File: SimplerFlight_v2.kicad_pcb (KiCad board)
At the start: 2 copper layers, 93.8 x 73.5 mm, 77 parts, among them J1 Battery 1, J11 Servo, J13 SWD Header, J14 DM3CS-SF, J2 Encoder, J7 Battery 2, J8 USB, Q2 NPN, SW1 Boot Switch, SW2 System Reset, U1 AMS1117-3.3, U2 STM32F401RETx, U3 BMP581, U4 BNO085, U5 TPS56A37RPAR, U7 MX25V4006EM1I-13G, Y2 Crystal

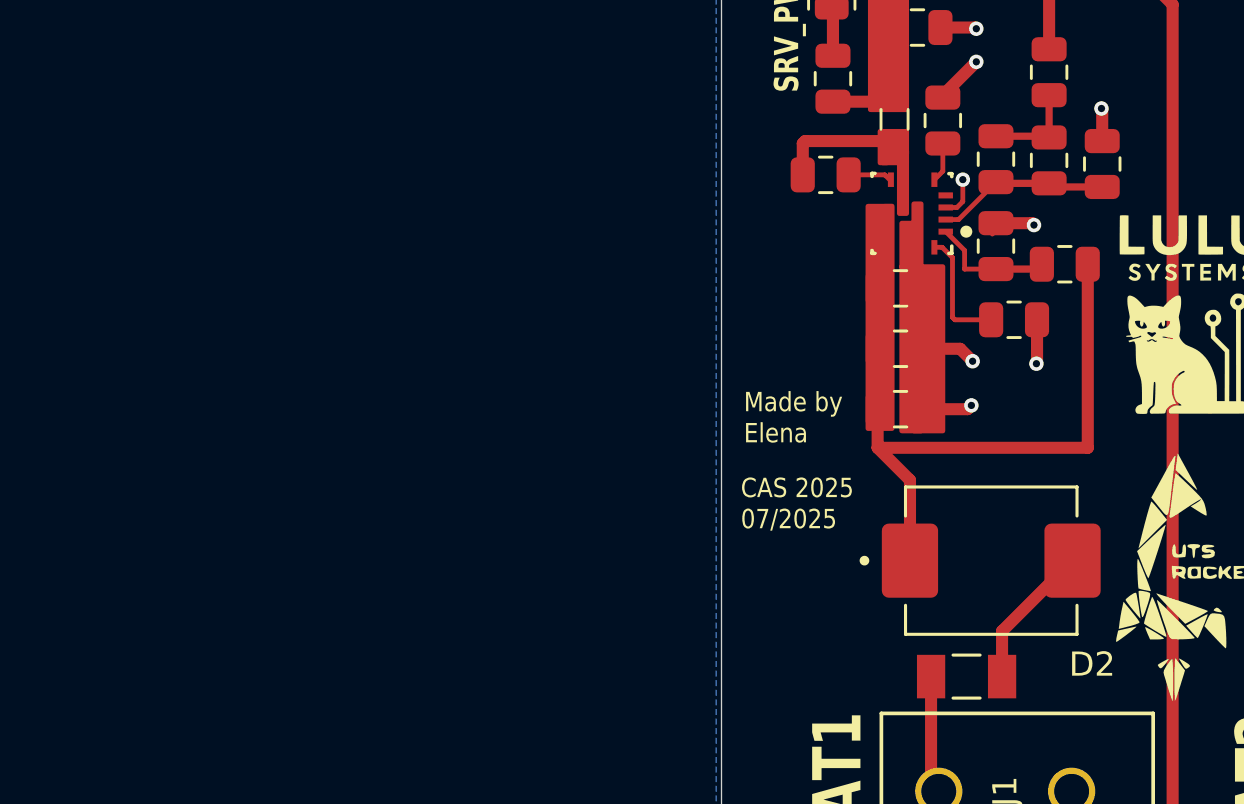
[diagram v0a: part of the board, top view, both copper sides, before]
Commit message: remove redundant current sensing
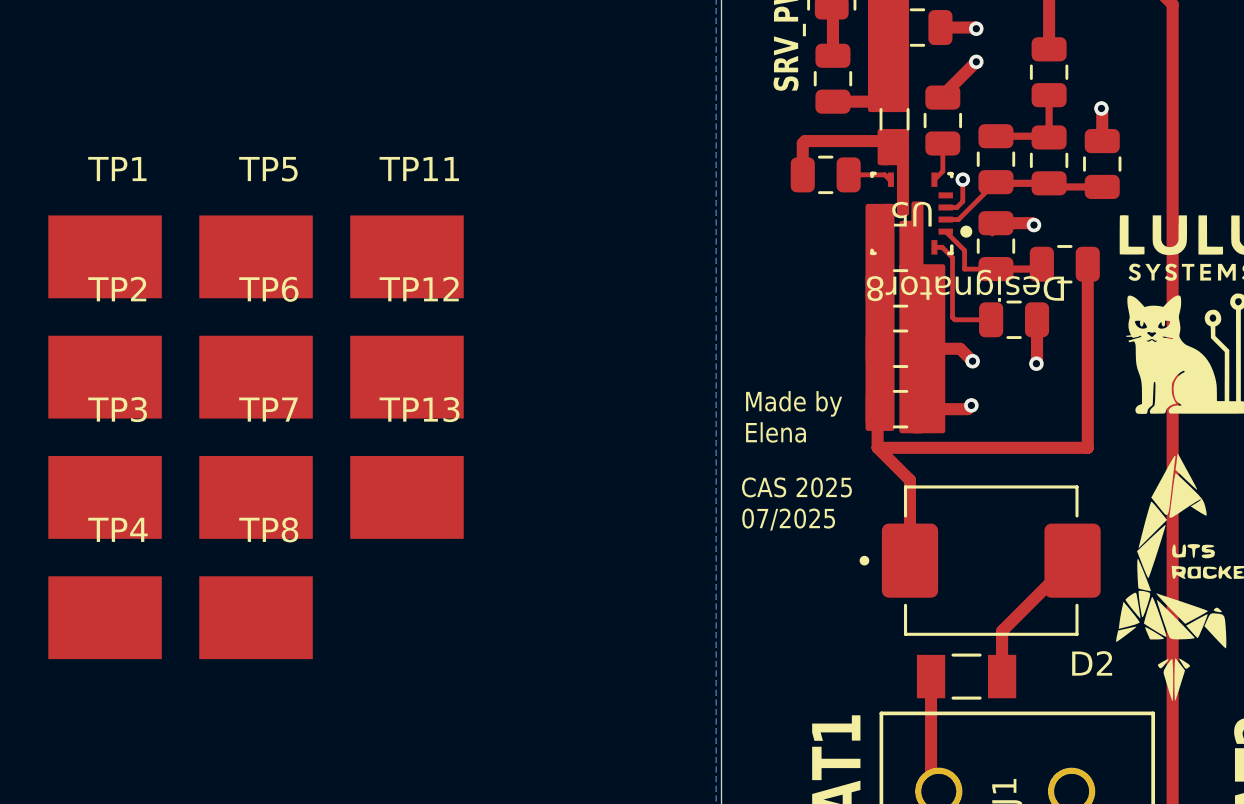
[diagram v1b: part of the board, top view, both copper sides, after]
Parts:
- added TP1: 5016, 5016:KEYSTONE_5016, F.Cu at (119.5, 102.5)
- added TP11: 5016, 5016:KEYSTONE_5016, F.Cu at (132.0, 102.5)
- added TP12: 5016, 5016:KEYSTONE_5016, F.Cu at (132.0, 107.4)
- added TP13: 5016, 5016:KEYSTONE_5016, F.Cu at (132.0, 112.4)
- added TP2: 5016, 5016:KEYSTONE_5016, F.Cu at (119.5, 107.4)
- added TP3: 5016, 5016:KEYSTONE_5016, F.Cu at (119.5, 112.4)
- added TP4: 5016, 5016:KEYSTONE_5016, F.Cu at (119.5, 117.4)
- added TP5: 5016, 5016:KEYSTONE_5016, F.Cu at (125.7, 102.5)
- added TP6: 5016, 5016:KEYSTONE_5016, F.Cu at (125.7, 107.4)
- added TP7: 5016, 5016:KEYSTONE_5016, F.Cu at (125.7, 112.4)
- added TP8: 5016, 5016:KEYSTONE_5016, F.Cu at (125.7, 117.4)
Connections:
- U2 pad 16: /Microcontroller/USART2_TX -> unconnected-(U2-PA2-Pad16)
- U2 pad 17: /Microcontroller/USART2_RX -> unconnected-(U2-PA3-Pad17)
- U2 pad 37: /Microcontroller/USART6_TX -> unconnected-(U2-PC6-Pad37)
- U2 pad 38: /Microcontroller/USART6_RX -> unconnected-(U2-PC7-Pad38)
- U2 pad 51: /Microcontroller/CAM_1_EN -> unconnected-(U2-PC10-Pad51)
- U2 pad 52: /Microcontroller/CAM_2_EN -> unconnected-(U2-PC11-Pad52)
- U2 pad 53: /Microcontroller/CAM_3_EN -> unconnected-(U2-PC12-Pad53)
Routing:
- net (no net): track 0.00 -> 0.62 mm

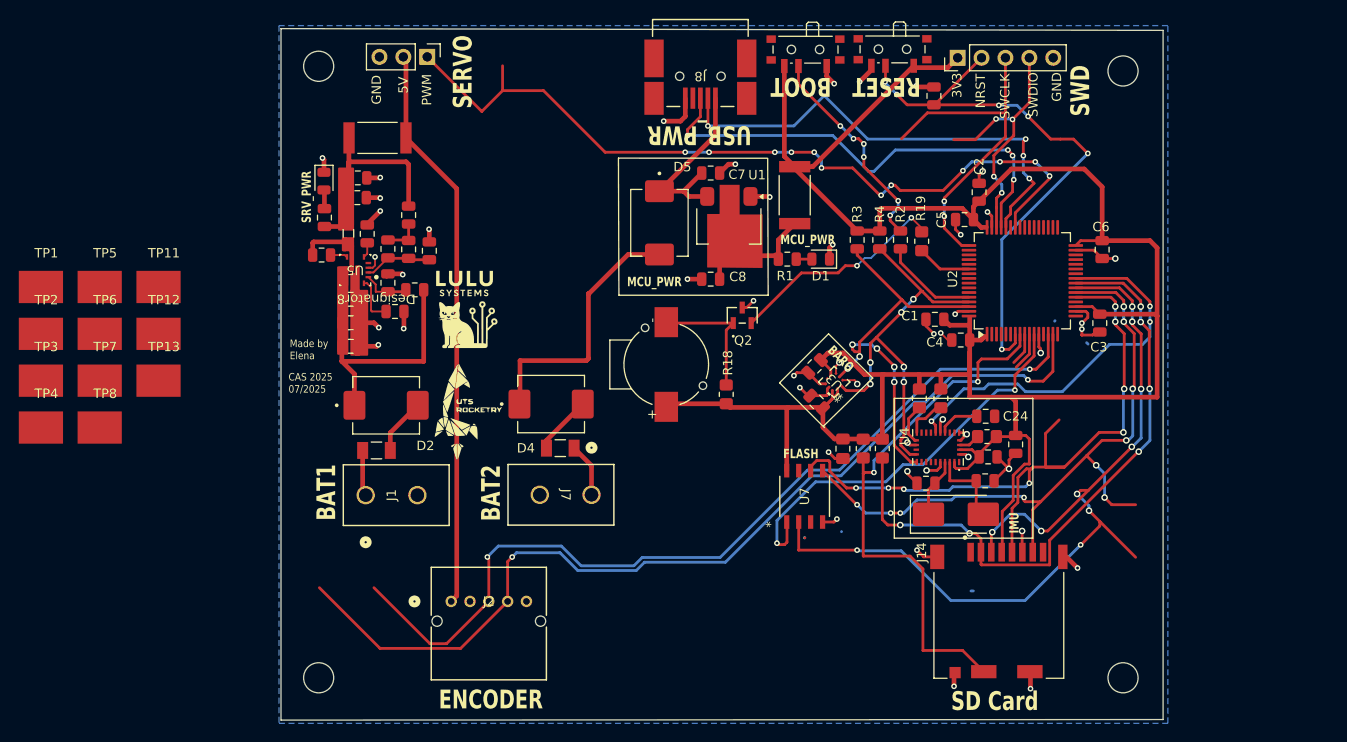
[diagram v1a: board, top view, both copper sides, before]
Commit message: make pcb footprint smaller
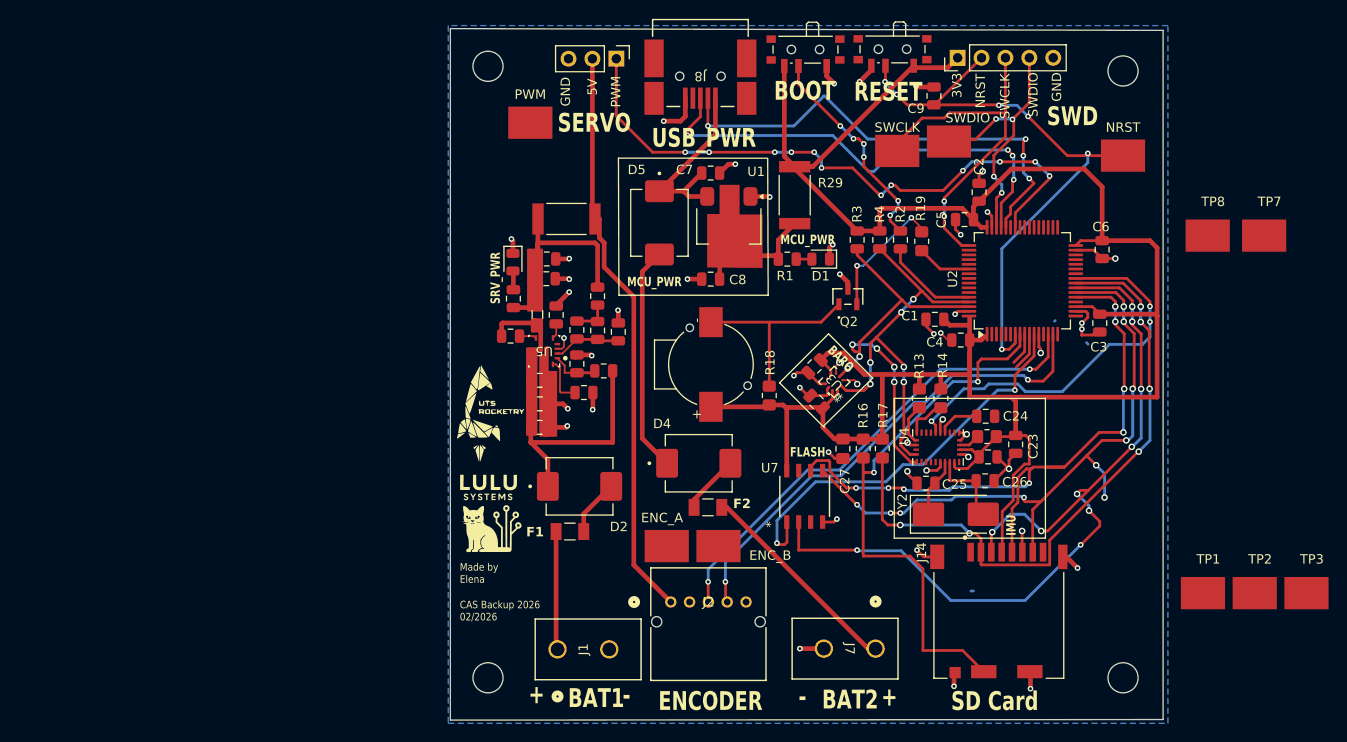
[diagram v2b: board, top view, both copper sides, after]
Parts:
- moved TP3 136.4 mm to (254.0, 135.0)
- moved TP2 131.9 mm to (248.5, 135.0)
- moved TP1 127.7 mm to (243.0, 135.0)
- moved TP7 124.7 mm to (249.5, 97.0)
- moved TP8 119.5 mm to (243.5, 97.0)
- moved NRST 110.4 mm to (234.5, 88.5)
- moved SWDIO 101.2 mm to (216.0, 87.0)
- moved SWCLK 86.0 mm to (210.5, 88.0)
- moved ENC_B 63.7 mm to (191.5, 130.0)
- moved ENC_A 56.8 mm to (186.0, 130.0)
- moved PWM 43.2 mm to (171.5, 85.0)
- moved J7 34.3 mm to (208.2, 140.9)
- moved J1 26.2 mm to (174.4, 141.0)
- moved J2 23.3 mm to (186.4, 135.9)
- moved F1 22.3 mm to (175.7, 128.5)
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- renumbered TP13 to ENC_A, TP12 to ENC_B, TP6 to NRST, TP11 to PWM, TP5 to SWCLK, TP4 to SWDIO
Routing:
- net /Microcontroller/ENC_B: track 101.3 -> 52.0 mm
- net /Microcontroller/ENC_A: track 93.9 -> 51.4 mm
- net /Microcontroller/SERVO_PWM: track 86.8 -> 65.7 mm
- net Net-(F2-Pad1): track 5.72 -> 22.6 mm
- net Net-(Q2-B): track 23.8 -> 14.0 mm
- net Net-(F1-Pad1): track 4.88 -> 12.6 mm
- net Net-(Q2-C): track 14.0 -> 21.2 mm
- net /Microcontroller/SPI1_SCK: track 75.5 -> 69.9 mm
- net /Microcontroller/SPI1_MOSI: track 96.8 -> 91.4 mm
- net /Headers/+3V3: track 250.1 -> 245.2 mm
- net Net-(D4-PadC): track 28.2 -> 24.0 mm
- net NRST: track 60.9 -> 64.9 mm
- net /Microcontroller/SPI1_MISO: track 73.9 -> 70.2 mm
- net GND: track 100.2 -> 103.2 mm, vias 47 -> 48
- net /Peripherals/5V_SERVO: track 60.5 -> 61.2 mm
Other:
- board size 93.8 x 73.5 mm -> 75.8 x 73.5 mm
- board text added: "+"
- board text added: "-"
- board text added: "CAS Backup 2026 02/2026"
- board text removed: "CAS 2025 07/2025"
